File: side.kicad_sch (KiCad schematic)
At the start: 85 parts, among them J1 Conn_01x02, J2 SWD_Connector, J3 USB_C_Receptacle_USB2.0_16P, SW1 Reset Button, SW10 SW_Push, SW11 SW_Push, SW12 SW_Push, SW13 SW_Push, SW14 SW_Push, SW15 SW_Push, SW16 SW_Push, SW17 SW_Push, SW18 SW_Push, SW19 SW_Push, SW2 SW_On_Off, SW20 SW_Push, SW21 SW_Push, SW22 SW_Push, SW23 SW_Push, SW3 SW_Push, SW4 SW_Push, SW5 SW_Push, SW6 SW_Push, SW7 SW_Push, SW8 SW_Push, SW9 SW_Push, U2 USBLC6-2SC6, U7 nRF52833_QDxx, Y1 32MHz, Y3 32.768 kHz

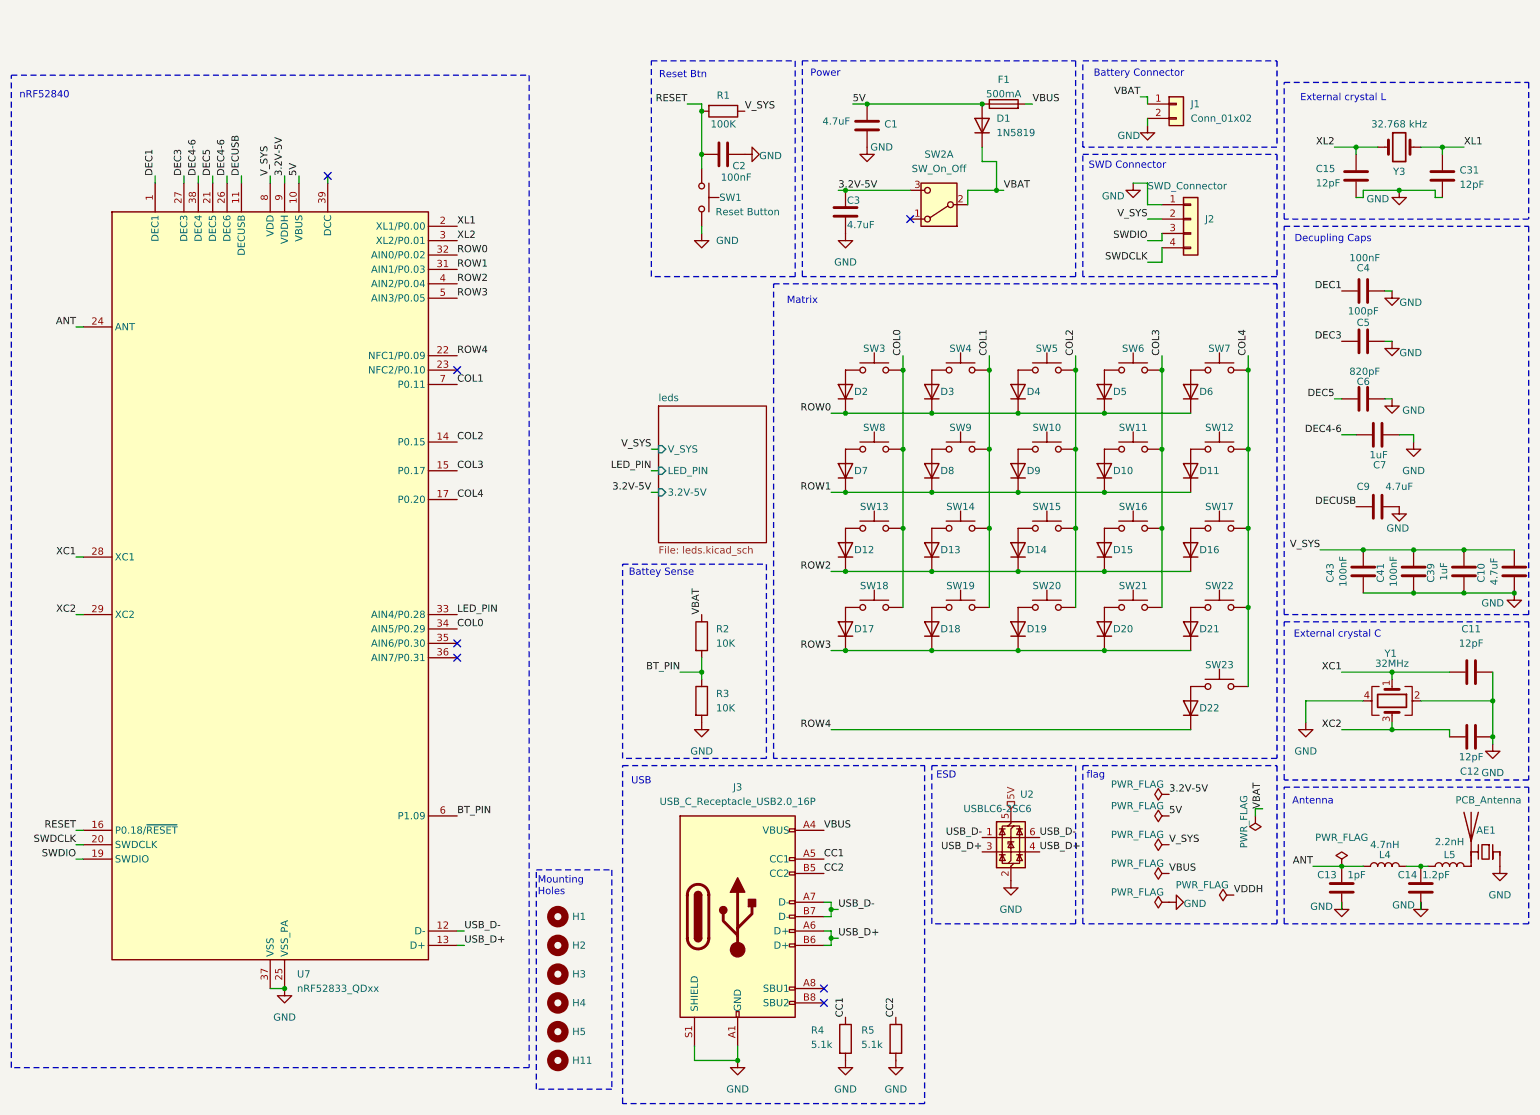
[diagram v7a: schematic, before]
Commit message: adding power and battery management
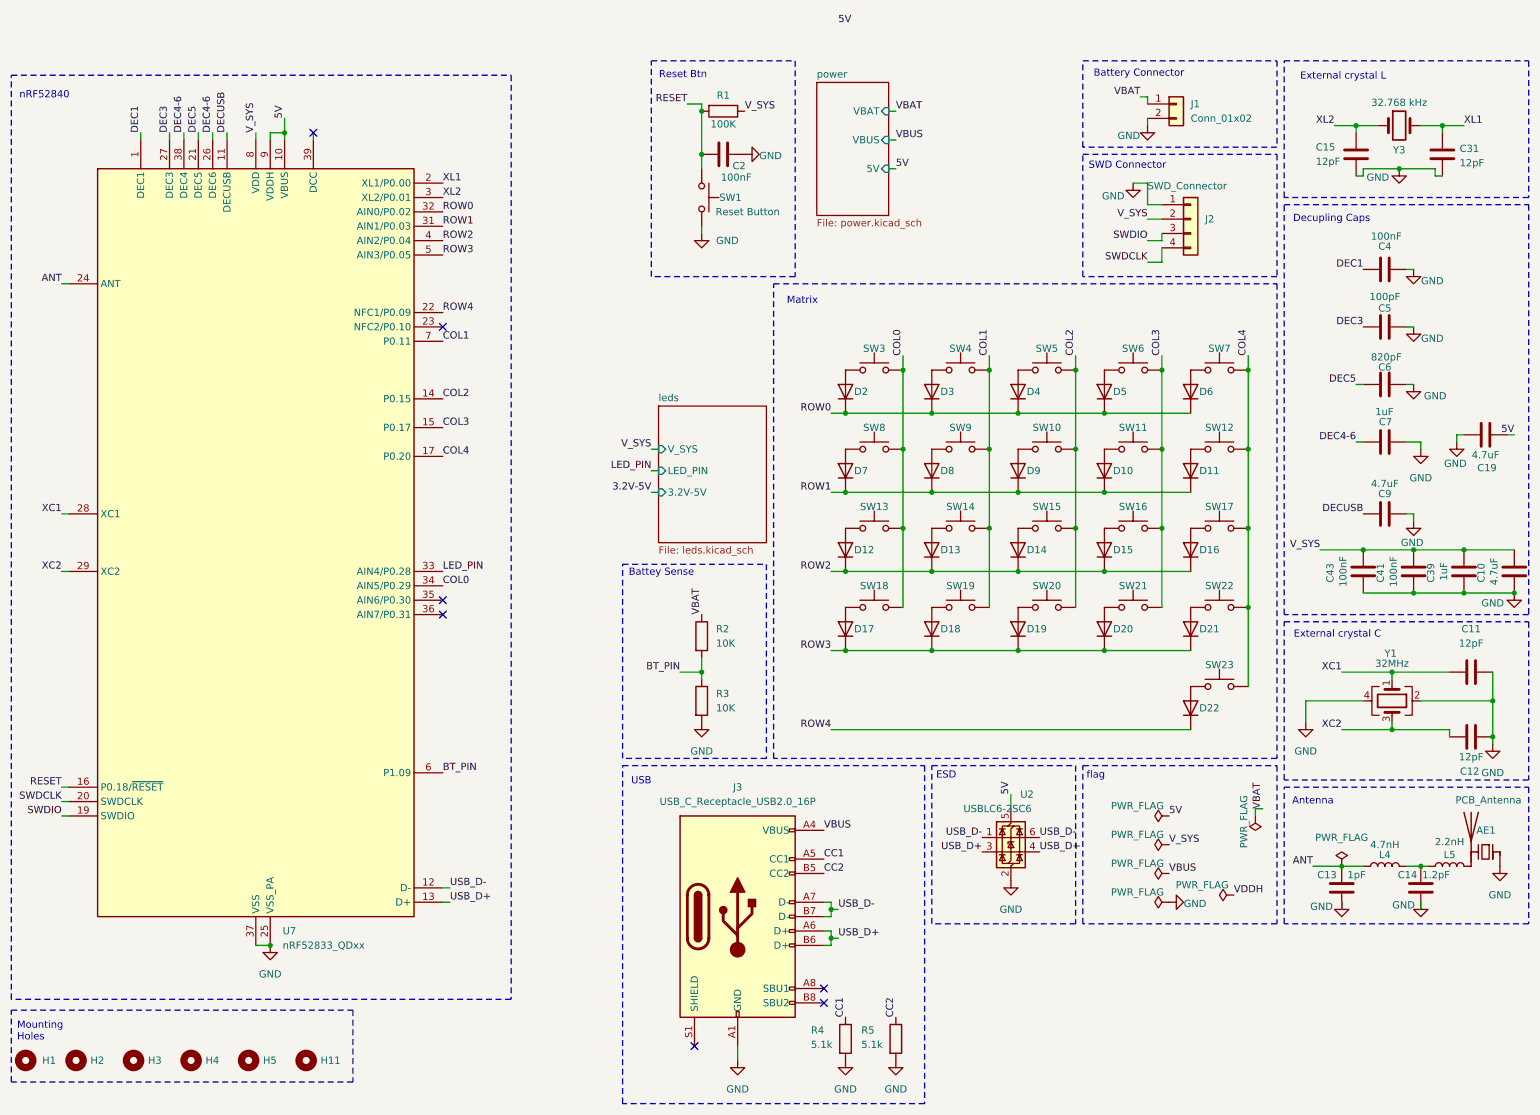
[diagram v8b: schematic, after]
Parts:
- removed C1, C3: 4.7uF, Capacitor_SMD:C_0603_1608Metric, symbol Device:C
- removed D1: 1N5819, Diode_SMD:D_SOD-123, symbol Device:D
- removed F1: 500mA, Fuse:Fuse_0603_1608Metric, symbol Device:Fuse
- removed SW2: SW_On_Off, Button_Switch_THT:SW_CK_JS202011AQN_DPDT_Angled, symbol Switch:SW_DPDT_x2
- added C19: 4.7uF, Capacitor_SMD:C_0603_1608Metric, symbol Device:C
- J3: LCSC C963213 -> C2988369
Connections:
- net 3.2V-5V: no longer U7.9 (VDDH)
- net 5V: now also U7.9 (VDDH), C19.1
- net GND: now also C19.2; no longer J3.S1 (SHIELD)
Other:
- added sheet power (power.kicad_sch)
- note removed: "Power"
- moved on the sheet: C15, C31, C4, C5, C6, C7, C9, H1, H11, H2, H3, H4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
